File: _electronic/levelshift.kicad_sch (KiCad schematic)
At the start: 10 parts

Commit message: BETA first upload
nothing major done here:
* updated KiCAD files to v9
* removed alternative 6v feed-in. The proposed buck converter is fine.
* added to all components LCSC component IDs. With this, exporting the project as gerber files also automatically creates correct BOM for JLCPCB manufacturing
*
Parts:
- D_HALL1, D_SERVO1: LCSC (none) -> C2290
- Q_HALL1, Q_SERVO1: LCSC (none) -> C83790
- R_HALL1, R_HALL2, R_SERVO1, R_SERVO2: LCSC (none) -> C25804
- R_HALL3, R_SERVO3: LCSC (none) -> C22775
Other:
- title: E-TKT v1.0 -> E-TKT v2.0 BETA

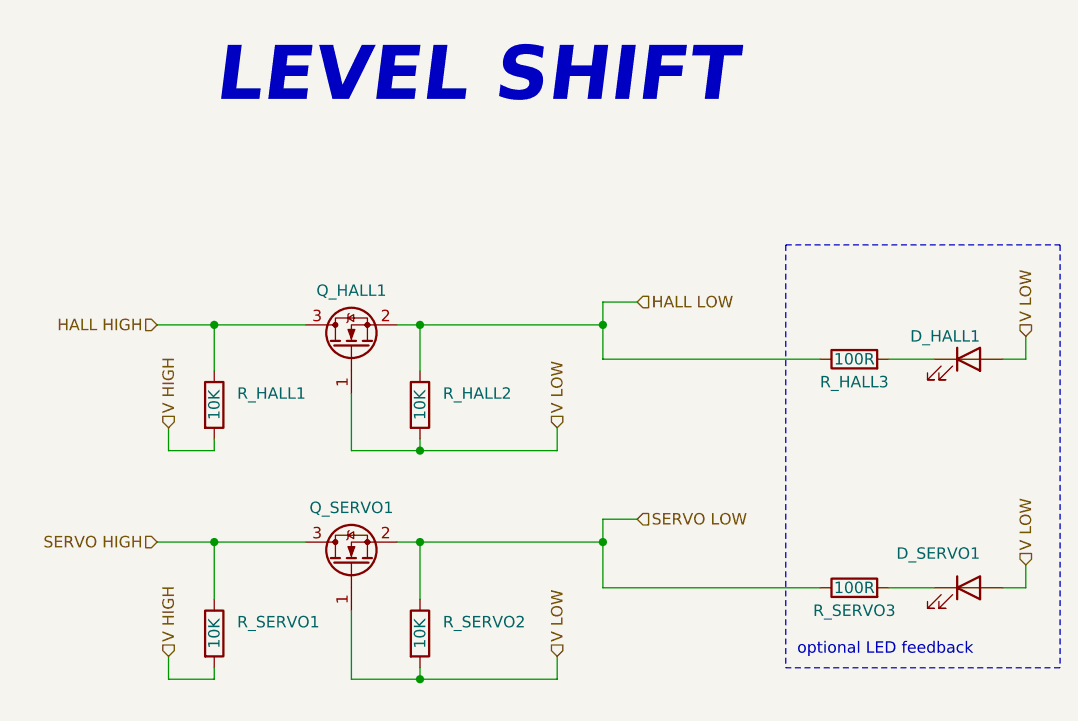
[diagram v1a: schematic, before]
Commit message: Updated layout of schematic symbol's text
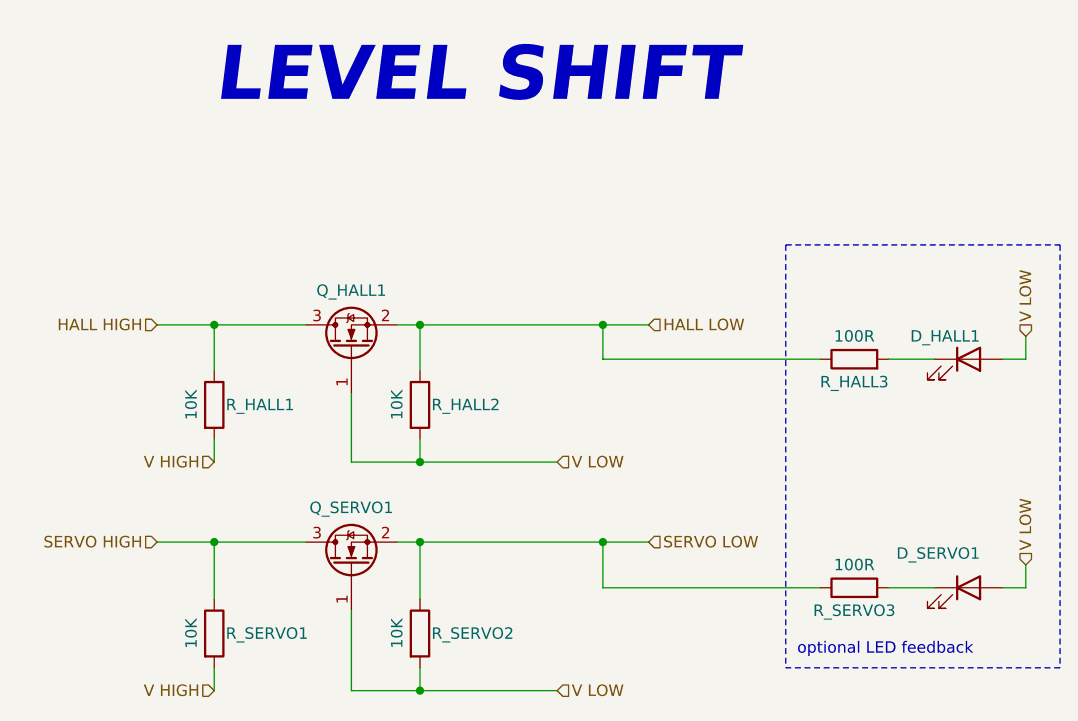
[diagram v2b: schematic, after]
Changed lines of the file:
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@@
 	)
 	(junction
-		(at 146.05 132.08)
+		(at 146.05 133.35)
 		(diameter 0)
 		(color 0 0 0 0)
@@
 	)
 	(junction
+		(at 146.05 107.95)
+		(diameter 0)
+		(color 0 0 0 0)
+	)
+	(junction
 		(at 166.37 92.71)
 		(diameter 0)
@@
 		(color 0 0 0 0)
 	)
-	(junction
-		(at 146.05 106.68)
-		(diameter 0)
-		(color 0 0 0 0)
-	)
 	(wire
 		(pts
@@
 	(wire
 		(pts
-			(xy 123.19 132.08) (xy 123.19 130.81)
-		)
-		(stroke
-			(width 0)
-			(type default)
-		)
-	)
-	(wire
-		(pts
-			(xy 138.43 124.46) (xy 138.43 132.08)
+			(xy 123.19 130.81) (xy 123.19 133.35)
+		)
+		(stroke
+			(width 0)
+			(type default)
+		)
+	)
+	(wire
+		(pts
+			(xy 138.43 124.46) (xy 138.43 133.35)
 		)
 		(stroke
@@
 	(wire
 		(pts
-			(xy 138.43 106.68) (xy 146.05 106.68)
+			(xy 146.05 105.41) (xy 146.05 107.95)
+		)
+		(stroke
+			(width 0)
+			(type default)
+		)
+	)
+	(wire
+		(pts
+			(xy 146.05 130.81) (xy 146.05 133.35)
+		)
+		(stroke
+			(width 0)
+			(type default)
+		)
+	)
+	(wire
+		(pts
+			(xy 138.43 107.95) (xy 146.05 107.95)
 		)
 		(stroke
@@
 	(wire
 		(pts
-			(xy 146.05 132.08) (xy 146.05 130.81)
-		)
-		(stroke
-			(width 0)
-			(type default)
-		)
-	)
-	(wire
-		(pts
 			(xy 123.19 116.84) (xy 133.35 116.84)
 		)
@@
 	(wire
 		(pts
-			(xy 166.37 114.3) (xy 166.37 116.84)
-		)
-		(stroke
-			(width 0)
-			(type default)
-		)
-	)
-	(wire
-		(pts
-			(xy 118.11 129.54) (xy 118.11 132.08)
-		)
-		(stroke
-			(width 0)
-			(type default)
-		)
-	)
-	(wire
-		(pts
-			(xy 123.19 106.68) (xy 118.11 106.68)
-		)
-		(stroke
-			(width 0)
-			(type default)
-		)
-	)
-	(wire
-		(pts
-			(xy 166.37 114.3) (xy 170.18 114.3)
-		)
-		(stroke
-			(width 0)
-			(type default)
-		)
-	)
-	(wire
-		(pts
-			(xy 138.43 132.08) (xy 146.05 132.08)
+			(xy 166.37 116.84) (xy 171.45 116.84)
+		)
+		(stroke
+			(width 0)
+			(type default)
+		)
+	)
+	(wire
+		(pts
+			(xy 138.43 133.35) (xy 146.05 133.35)
 		)
 		(stroke
@@
 	(wire
 		(pts
-			(xy 138.43 100.33) (xy 138.43 106.68)
-		)
-		(stroke
-			(width 0)
-			(type default)
-		)
-	)
-	(wire
-		(pts
-			(xy 118.11 132.08) (xy 123.19 132.08)
+			(xy 138.43 100.33) (xy 138.43 107.95)
 		)
 		(stroke
@@
 	(wire
 		(pts
-			(xy 123.19 105.41) (xy 123.19 106.68)
+			(xy 123.19 105.41) (xy 123.19 107.95)
 		)
 		(stroke
@@
 	(wire
 		(pts
-			(xy 161.29 129.54) (xy 161.29 132.08)
-		)
-		(stroke
-			(width 0)
-			(type default)
-		)
-	)
-	(wire
-		(pts
-			(xy 118.11 104.14) (xy 118.11 106.68)
-		)
-		(stroke
-			(width 0)
-			(type default)
-		)
-	)
-	(wire
-		(pts
-			(xy 170.18 90.17) (xy 166.37 90.17)
+			(xy 171.45 92.71) (xy 166.37 92.71)
 		)
 		(stroke
@@
 	(wire
 		(pts
-			(xy 146.05 106.68) (xy 161.29 106.68)
+			(xy 146.05 107.95) (xy 161.29 107.95)
 		)
 		(stroke
@@
 	(wire
 		(pts
-			(xy 161.29 106.68) (xy 161.29 104.14)
-		)
-		(stroke
-			(width 0)
-			(type default)
-		)
-	)
-	(wire
-		(pts
 			(xy 210.82 96.52) (xy 213.36 96.52)
 		)
@@
 	(wire
 		(pts
-			(xy 166.37 90.17) (xy 166.37 92.71)
-		)
-		(stroke
-			(width 0)
-			(type default)
-		)
-	)
-	(wire
-		(pts
-			(xy 146.05 132.08) (xy 161.29 132.08)
-		)
-		(stroke
-			(width 0)
-			(type default)
-		)
-	)
-	(wire
-		(pts
-			(xy 146.05 106.68) (xy 146.05 105.41)
+			(xy 146.05 133.35) (xy 161.29 133.35)
 		)
 		(stroke
@@
 	(hierarchical_label "V LOW"
 		(shape input)
-		(at 161.29 129.54 90)
+		(at 161.29 133.35 0)
 		(effects
 			(font
@@
 	(hierarchical_label "SERVO LOW"
 		(shape input)
-		(at 170.18 114.3 0)
+		(at 171.45 116.84 0)
 		(effects
 			(font
@@
 	(hierarchical_label "V HIGH"
 		(shape input)
-		(at 118.11 129.54 90)
+		(at 123.19 133.35 180)
 		(effects
 			(font
 				(size 1.27 1.27)
 			)
-			(justify left)
+			(justify right)
 		)
 	)
 	(hierarchical_label "V LOW"
 		(shape input)
-		(at 161.29 104.14 90)
+		(at 161.29 107.95 0)
 		(effects
 			(font
@@
 	(hierarchical_label "V HIGH"
 		(shape input)
-		(at 118.11 104.14 90)
+		(at 123.19 107.95 180)
 		(effects
 			(font
 				(size 1.27 1.27)
 			)
-			(justify left)
+			(justify right)
 		)
 	)
 	(hierarchical_label "HALL LOW"
 		(shape input)
-		(at 170.18 90.17 0)
+		(at 171.45 92.71 0)
 		(effects
 			(font
@@
 		)
 		(property "Value" "100R"
-			(at 194.31 96.52 90)
+			(at 194.31 93.98 90)
 			(effects
 				(font
@@
 		(dnp no)
 		(property "Reference" "R_HALL1"
-			(at 125.73 100.3299 0)
+			(at 124.46 101.6 0)
 			(effects
 				(font
@@
 		)
 		(property "Value" "10K"
-			(at 123.19 101.6 90)
+			(at 120.65 101.6 90)
 			(effects
 				(font
@@
 		(dnp no)
 		(property "Reference" "R_SERVO1"
-			(at 125.73 125.7299 0)
+			(at 124.46 127 0)
 			(effects
 				(font
@@
 		)
 		(property "Value" "10K"
-			(at 123.19 127 90)
+			(at 120.65 127 90)
 			(effects
 				(font
@@
 		)
 		(property "Value" "100R"
-			(at 194.31 121.92 90)
+			(at 194.31 119.38 90)
 			(effects
 				(font
@@
 		(dnp no)
 		(property "Reference" "R_SERVO2"
-			(at 148.59 125.7299 0)
+			(at 147.32 127 0)
 			(effects
 				(font
@@
 		)
 		(property "Value" "10K"
-			(at 146.05 127 90)
+			(at 143.51 127 90)
 			(effects
 				(font
@@
 		(dnp no)
 		(property "Reference" "R_HALL2"
-			(at 148.59 100.3299 0)
+			(at 147.32 101.6 0)
 			(effects
 				(font
@@
 		)
 		(property "Value" "10K"
-			(at 146.05 101.6 90)
-			(effects
-				(font
+			(at 143.51 101.6 90)
+			(effects
+				(font
